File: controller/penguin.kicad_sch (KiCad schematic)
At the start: 155 parts, among them IC1 HY2120-AB, J1 USB_C_CONN, J10 MTR_HEADER_2, J2 CAM_HEADER, J3 BATT_BALANCE_HEADER, J4 TOF_HEADER, J5 I2C_JUMPER, J6 I2C_JUMPER, J7 SERVO_CONN, J8 BATT_CONN, J9 MTR_HEADER_1, Q1 AO3400A, Q2 SI2393DS, Q3 2N7002, Q4 FS8205A, SW1 SW_Boot, SW2 SW_Reset, U1 ESP32-S3-WROOM-1U-N8R8, U10 TPS62143, U2 LP5907MFX-2.8, U3 LP5907MFX-1.2, U4 DRV8833PW, U5 MCP23017_ML, U6 TPS5405DR, U7 AMS1117-3.3, U8 DMP4065S-7, U9 LSM6DSL

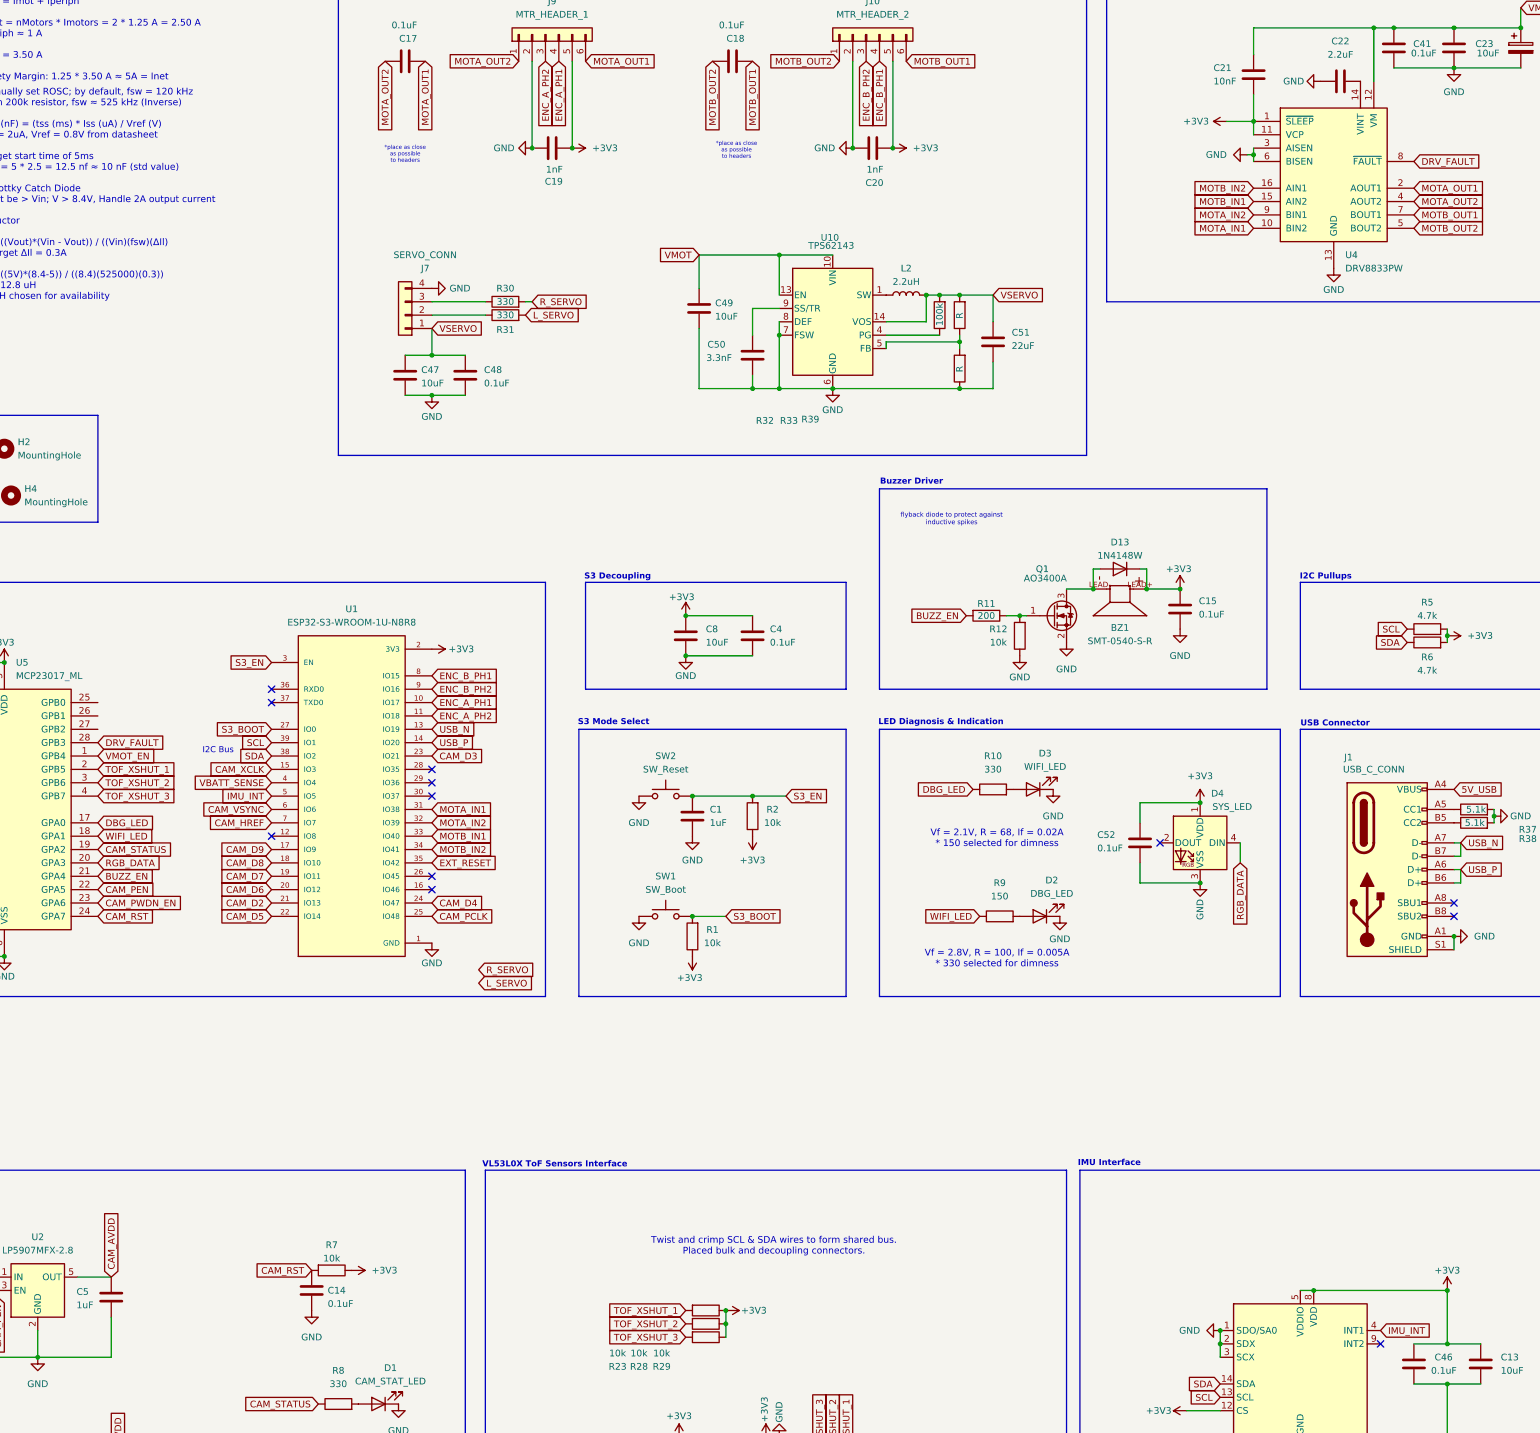
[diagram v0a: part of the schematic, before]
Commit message: added servo
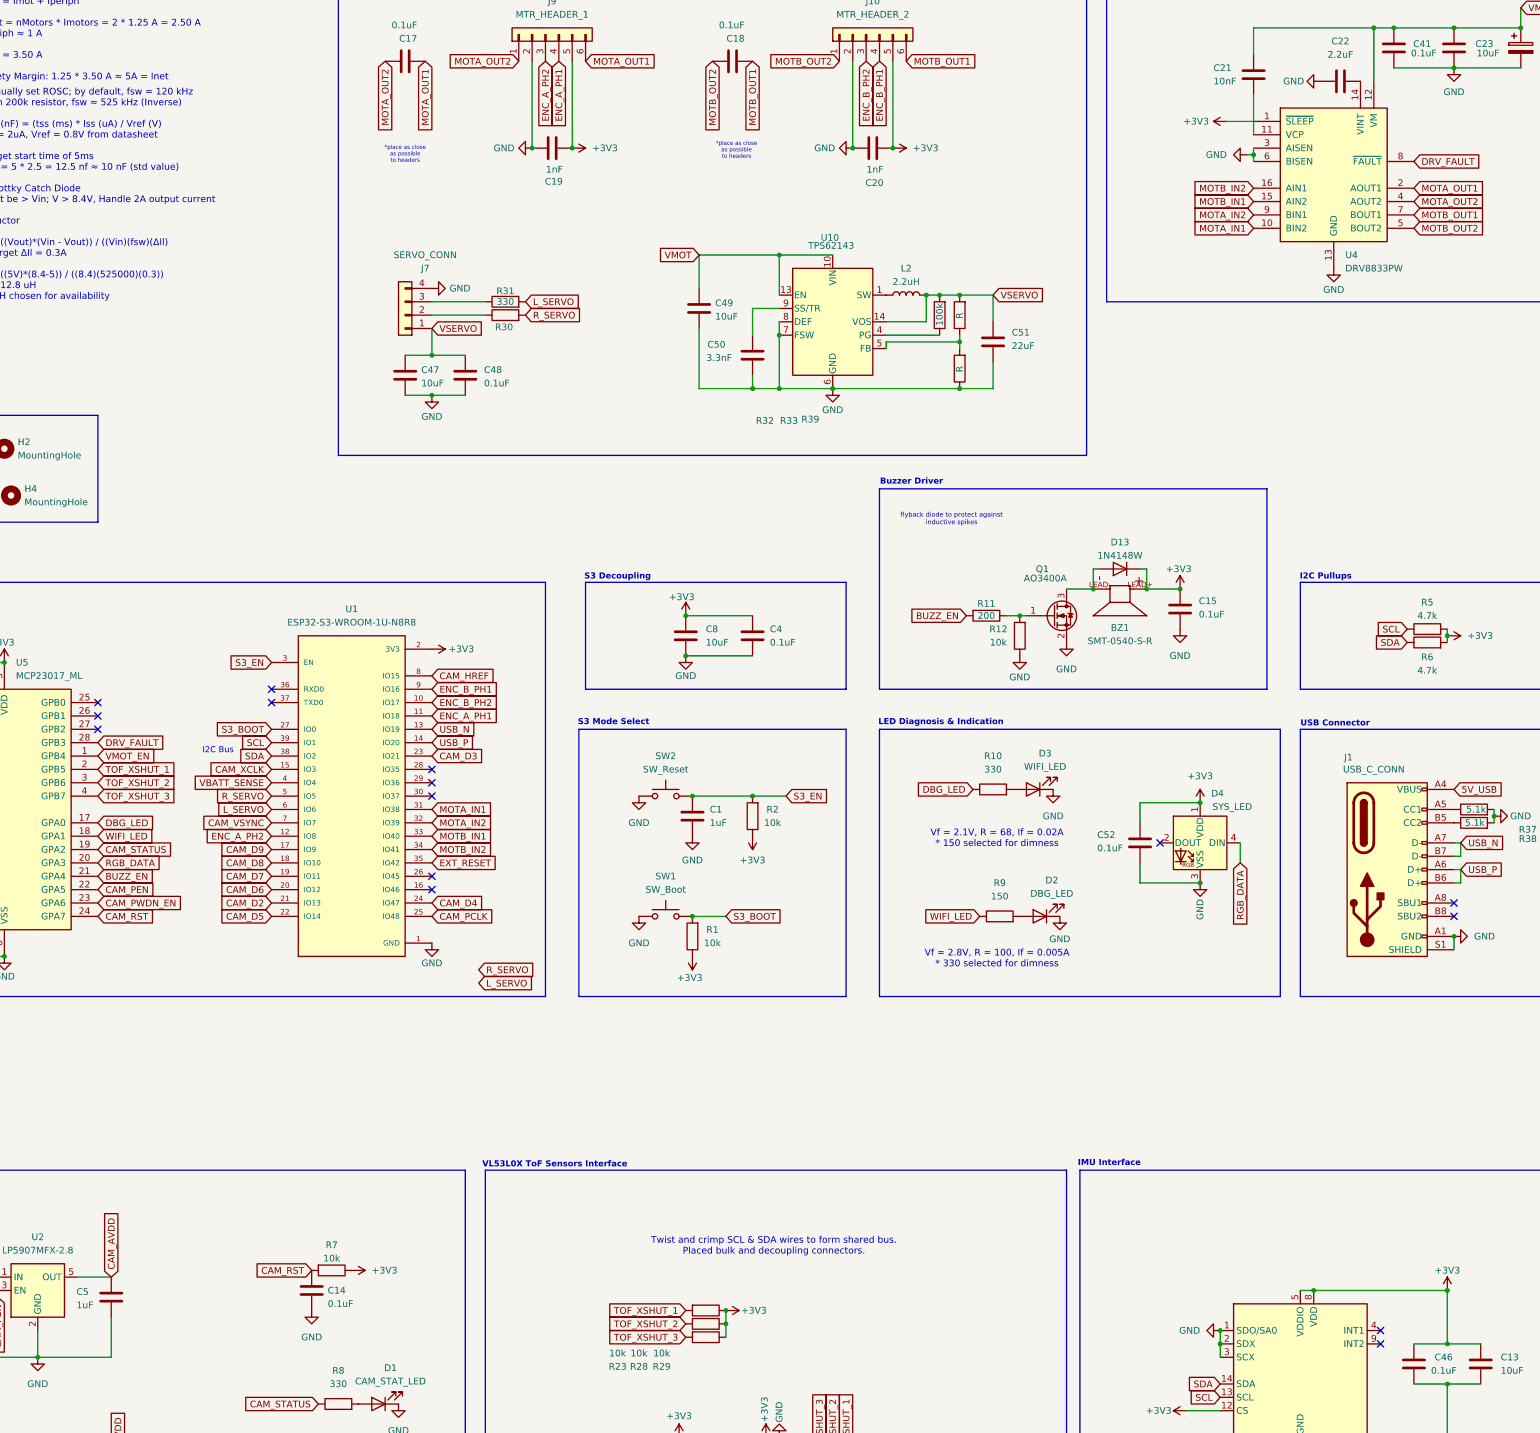
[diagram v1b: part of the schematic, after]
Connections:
- net +3V3: no longer C21.2, U4.11 (VCP)
- net CAM_HREF: now also U1.8 (IO15); no longer U1.7 (IO7)
- net CAM_VSYNC: now also U1.7 (IO7); no longer U1.6 (IO6)
- net ENC_A_PH1: now also U1.11 (IO18); no longer U1.10 (IO17)
- net ENC_A_PH2: now also U1.12 (IO8); no longer U1.11 (IO18)
- net ENC_B_PH1: now also U1.9 (IO16); no longer U1.8 (IO15)
- net ENC_B_PH2: now also U1.10 (IO17); no longer U1.9 (IO16)
- net L_SERVO: now also U1.6 (IO6)
- net R_SERVO: now also U1.5 (IO5)
- net at J7.2 (Pin_2): now also R30.1; no longer R31.1
- net at J7.3 (Pin_3): now also R31.1; no longer R30.1
- net IMU_INT: no longer names the net of U9.4 (INT1)
- net IMU_INT: no longer U1.5 (IO5)
- new net: C21.2, U4.11 (VCP)
- no-connect marks 17 -> 20

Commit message: finish hardware review
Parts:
- removed R39: R, Resistor_SMD:R_0402_1005Metric, symbol Device:R
- added D14: SERVO_V_LED, LED_SMD:LED_0603_1608Metric, symbol Device:LED
- added R40: 330, Resistor_SMD:R_0402_1005Metric, symbol Device:R
- added TP13: VSERVO_TP_PAD, TestPoint:TestPoint_Pad_1.0x1.0mm, symbol Connector:TestPoint
- BZ1, D4, D5, F1, J10, J3, J4, J8, J9: now not fitted
- C24: Digikey PCE4320TR-ND -> ZK1V101XV; now not fitted
- C40: Digikey P123721TR-ND -> ZK1V101XV; now not fitted
- D10: footprint LED_SMD:LED_0805_2012Metric -> LED_SMD:LED_0603_1608Metric; JLCPCB (none) -> C2289; LCSC C2297 -> (none)
- J5, J6: JLCPCB (none) -> C6333215
- J7: Digikey (none) -> WM14974-ND; now not fitted
- L2: JLCPCB (none) -> C5521727
- R16: value 180k -> 100k; JLCPCB C25811 -> C25803
- R19: value 1.2k -> 680; JLCPCB C22765 -> C23228
- R20: value 1k -> 680; JLCPCB C21190 -> C23228
- R21: value 330 -> 200; footprint Resistor_SMD:R_0402_1005Metric -> Resistor_SMD:R_0603_1608Metric; JLCPCB C25104 -> C8218
- R33: value R -> 10k; JLCPCB (none) -> C25744
- R37, R38: JLCPCB (none) -> C23186
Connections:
- net 5V_USB: now also R20.2; no longer R20.1
- net GND: now also R16.2, R33.1, U10.5 (FB), D14.1 (K); no longer R16.1
- net VSERVO: now also R40.1, TP13.1; no longer R33.2
- net at U6.3 (ROSC): now also R16.1; no longer R16.2
- net at D11.2 (A): now also R20.1; no longer R20.2
- net at J2.1 (Pin_1): now also R33.2
- new net: D14.2 (A), R40.2
- no-connect marks 20 -> 19
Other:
- moved on the sheet: C11, C51, D10, R19, TP11

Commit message: prod
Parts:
- BZ1, D4, D5: now fitted
- C1: JLCPCB C52923 -> (none); LCSC (none) -> C52923
- C10, C12, C14, C28, C33, C34, C36, C39, C4, C43, C44, C45, C46: JLCPCB C14663 -> (none); LCSC (none) -> C14663
- C11, C15, C16, C48, C52, C9: JLCPCB C1581 -> (none); LCSC (none) -> C1581
- C13, C23, C31, C35, C42, C47, C49, C8: JLCPCB C15850 -> (none); LCSC (none) -> C15850
- C17, C18, C41: JLCPCB C14663 -> (none)
- C19, C20: JLCPCB C1588 -> (none)
- C2, C3, C38, C5, C6: JLCPCB C15849 -> (none); LCSC (none) -> C15849
- C21: footprint Resistor_SMD:R_0402_1005Metric -> Capacitor_SMD:C_0402_1005Metric; JLCPCB C15195 -> (none); LCSC (none) -> C15195
- C22: JLCPCB C12530 -> (none); LCSC (none) -> C12530
- C25, C7: JLCPCB C29277 -> (none); LCSC (none) -> C29277
- C26: JLCPCB C49678 -> (none); LCSC (none) -> C49678
- C27: JLCPCB C15195 -> (none); LCSC (none) -> C15195
- C29, C32, C37, C51: JLCPCB C49326779 -> (none); LCSC (none) -> C49326779
- C30, C50: JLCPCB C1565 -> (none); LCSC (none) -> C1536
- D1: JLCPCB C2290 -> (none); LCSC (none) -> C2290
- D10, D14: JLCPCB C2289 -> (none); LCSC (none) -> C2289
- D11, D12, D6, D9: JLCPCB C2297 -> (none); LCSC (none) -> C2297
- D13: JLCPCB C81598 -> (none); LCSC (none) -> C81598
- D2, R9: JLCPCB C72038 -> (none); LCSC (none) -> C72038
- D3: JLCPCB C72041 -> (none); LCSC (none) -> C72041
- D7: JLCPCB BZT52C12 -> (none); LCSC (none) -> BZT52C12
- D8: JLCPCB C8678 -> (none); LCSC (none) -> C8678
- FB1: JLCPCB C136227 -> (none); LCSC (none) -> C136227
- IC1: JLCPCB C116509 -> (none); LCSC (none) -> C116509
- J1: JLCPCB C5178541 -> (none)
- J2: JLCPCB C202112 -> (none); LCSC (none) -> C202112
- J5, J6: JLCPCB C6333215 -> (none); LCSC (none) -> C6333215
- L1: JLCPCB C187450 -> (none); LCSC (none) -> C187450
- L2: JLCPCB C5521727 -> (none); LCSC (none) -> C5521727
- Q1: JLCPCB C20917 -> (none); LCSC (none) -> C20917
- Q2: JLCPCB C41348109 -> (none); LCSC (none) -> C41348109
- Q3: JLCPCB C8545 -> (none)
- Q4: JLCPCB C908265 -> (none); LCSC (none) -> C908265
- R1, R12, R13, R17, R2, R23, R28, R29, R33, R7: JLCPCB C25744 -> (none); LCSC (none) -> C25744
- R10, R30, R31, R34, R35, R40, R8: JLCPCB C25104 -> (none); LCSC (none) -> C25104
- R11: JLCPCB C25087 -> (none); LCSC (none) -> C25087
- R14, R18, R36: JLCPCB C22765 -> (none); LCSC (none) -> C22765
- R15, R24: JLCPCB C25804 -> (none)
- R16, R25, R32: JLCPCB C25803 -> (none); LCSC (none) -> C25803
- R19, R20: JLCPCB C23228 -> (none); LCSC (none) -> C23228
- R21: JLCPCB C8218 -> (none); LCSC (none) -> C8218
- R22: JLCPCB C25804 -> (none); LCSC (none) -> C25804
- R26: JLCPCB C8218 -> (none)
- R27: JLCPCB C25819 -> (none); LCSC (none) -> C25819
- R3, R4: JLCPCB C25092 -> (none); LCSC (none) -> C25092
- R37, R38: JLCPCB C23186 -> (none)
- R5, R6: JLCPCB C25900 -> (none); LCSC (none) -> C25900
- SW1, SW2: JLCPCB C561514 -> (none); LCSC (none) -> C561514
- U1: JLCPCB C2980300 -> (none); LCSC (none) -> C2980300
- U10: JLCPCB C140242 -> (none); LCSC (none) -> C140242
- U2: JLCPCB C186700 -> (none); LCSC (none) -> C186700
- U3: JLCPCB C73478 -> (none); LCSC (none) -> C73478
- U4: JLCPCB C544801 -> (none); LCSC (none) -> C544801
- U5: JLCPCB C629439 -> (none); LCSC (none) -> C629439
- U6: JLCPCB C488409 -> (none); LCSC (none) -> C488409
- U7: JLCPCB C6186 -> (none); LCSC (none) -> C6186
- U8: JLCPCB C182476 -> (none)
- U9: JLCPCB C94048 -> (none); LCSC (none) -> C94048
- UE1, UE2: JLCPCB C2869734 -> (none); LCSC (none) -> C2869734

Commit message: remove DNP flags for pics
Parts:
- C24, C40, F1, J10, J3, J4, J7, J8, J9: now fitted
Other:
- moved on the sheet: C25, C26, D5, D7, FB1, Q2, R15

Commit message: motor docs
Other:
- note removed: "*place as close as possible to headers"
- note removed: "addr: 0x20"
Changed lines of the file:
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@@
 		)
 	)
-	(text "addr: 0x20"
-		(exclude_from_sim no)
-		(at 224.79 236.728 0)
-		(effects
-			(font
-				(size 1.27 1.27)
-				(color 5 5 5 1)
-			)
-		)
-	)
 	(text "VBATT Regulation"
 		(exclude_from_sim no)
@@
 			(font
 				(size 1.27 1.27)
-				(color 0 0 0 1)
+				(thickness 0.254)
+				(bold yes)
+				(color 195 236 231 1)
 			)
 		)
@@
 		)
 	)
-	(text "*place as close \nas possible \nto headers"
-		(exclude_from_sim no)
-		(at 380.492 84.328 0)
-		(effects
-			(font
-				(size 0.762 0.762)
-				(color 0 0 0 1)
-			)
-		)
-	)
 	(text "BATT_N -> BMS -> "
 		(exclude_from_sim no)
@@
 		)
 	)
-	(text "*place as close \nas possible \nto headers"
-		(exclude_from_sim no)
-		(at 317.5 85.09 0)
-		(effects
-			(font
-				(size 0.762 0.762)
-				(color 0 0 0 1)
-			)
-		)
-	)
 	(text "VBATT\n| \nSW\n|\n\n"
 		(exclude_from_sim no)
@@
 		)
 	)
-	(global_label "R_SERVO"
-		(shape input)
-		(at 331.47 240.03 0)
-		(fields_autoplaced yes)
-		(effects
-			(font
-				(size 1.27 1.27)
-			)
-			(justify left)
-		)
-		(property "Intersheetrefs" "${INTERSHEET_REFS}"
-			(at 342.7404 240.03 0)
-			(effects
-				(font
-					(size 1.27 1.27)
-				)
-				(justify left)
-				(hide yes)
-			)
-		)
-	)
 	(global_label "CAM_XCLK"
 		(shape input)
@@
 				(hide yes)
 			)
-		)
-	)
-	(global_label "L_SERVO"
-		(shape input)
-		(at 331.47 242.57 0)
-		(fields_autoplaced yes)
-		(effects
-			(font
-				(size 1.27 1.27)
-			)
-			(justify left)
-		)
-		(property "Intersheetrefs" "${INTERSHEET_REFS}"
-			(at 342.4985 242.57 0)
-			(effects
-				(font
-					(size 1.27 1.27)
-				)
-				(justify left)
-				(hide yes)
-			)
